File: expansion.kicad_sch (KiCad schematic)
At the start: 8 parts, among them J5 MEZZANINE, J7 PMOD_A, J8 PMOD_B

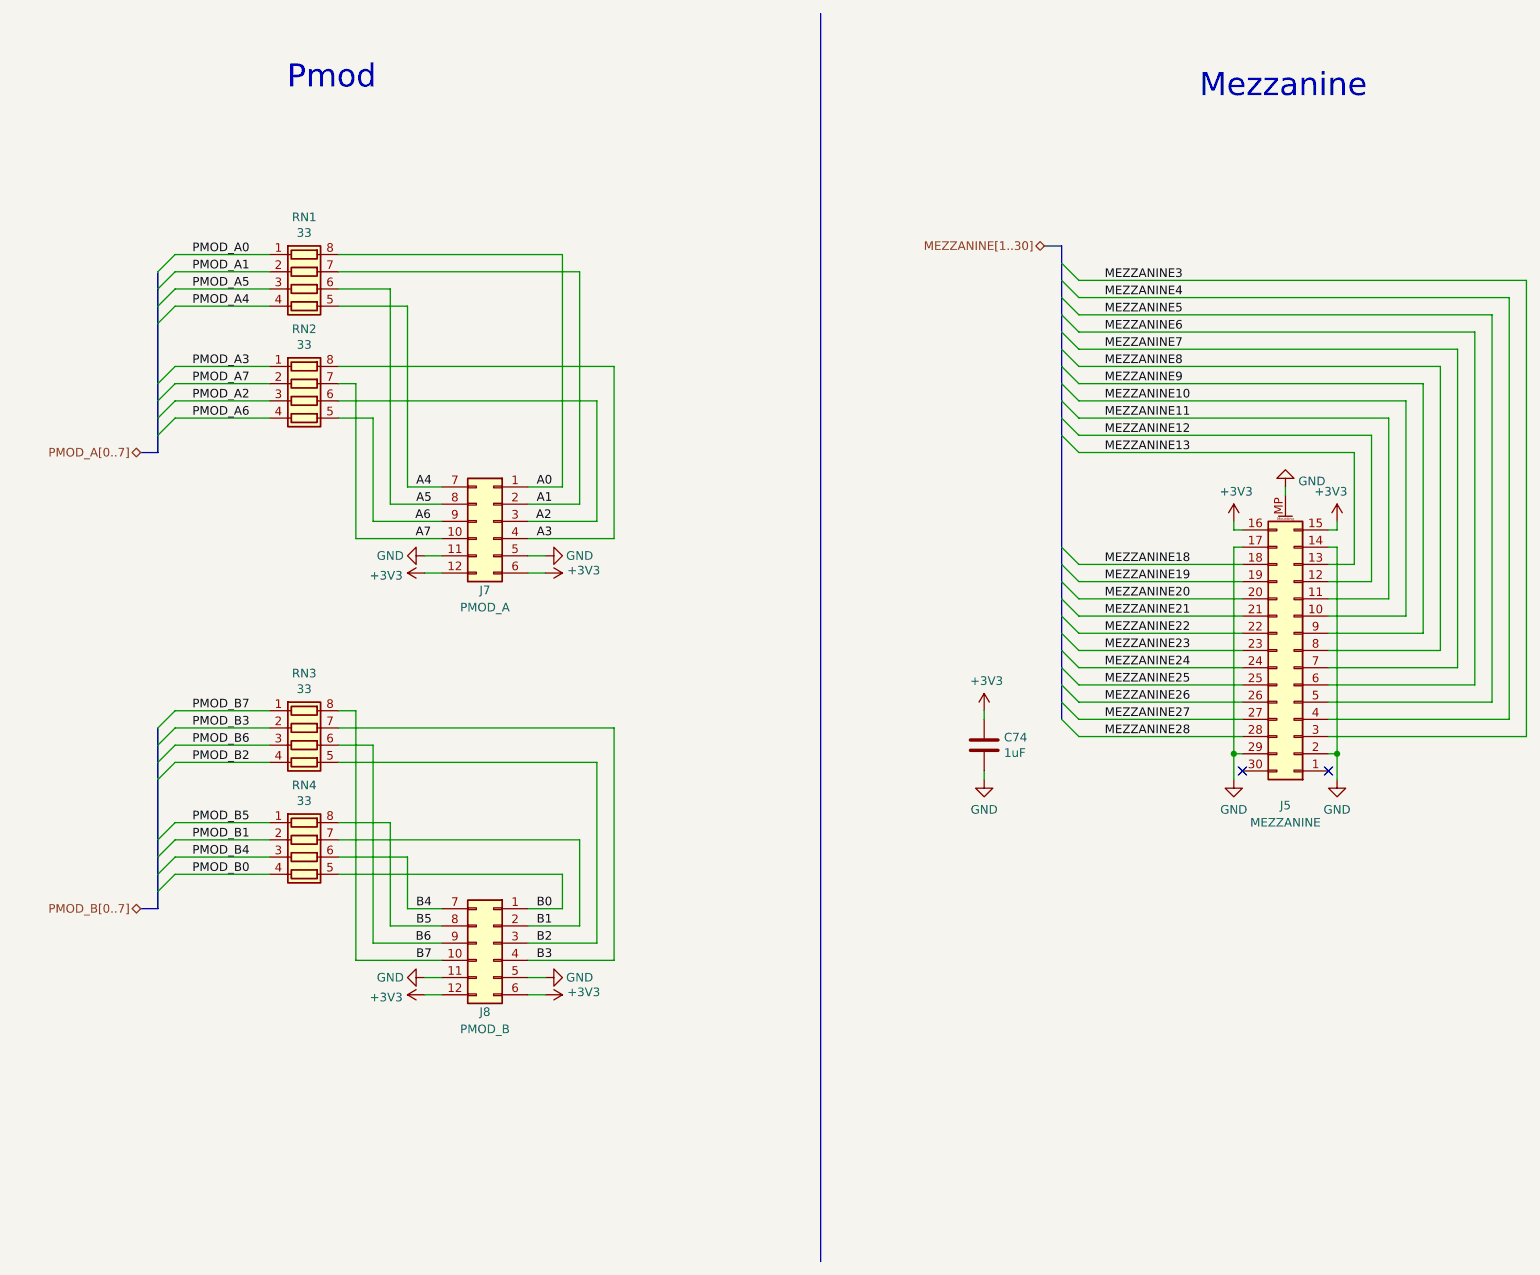
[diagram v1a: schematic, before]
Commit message: Clean up schematic
- Renumber Pmod signal names to match silkscreen labels
- Clean up FPGA symbol
- Clean up PHY symbol
- Add title block to newer sheets
- Fix horizontal line in LED sheet
- Improve various label positions
- Update data sheet fields
- Renumber pages
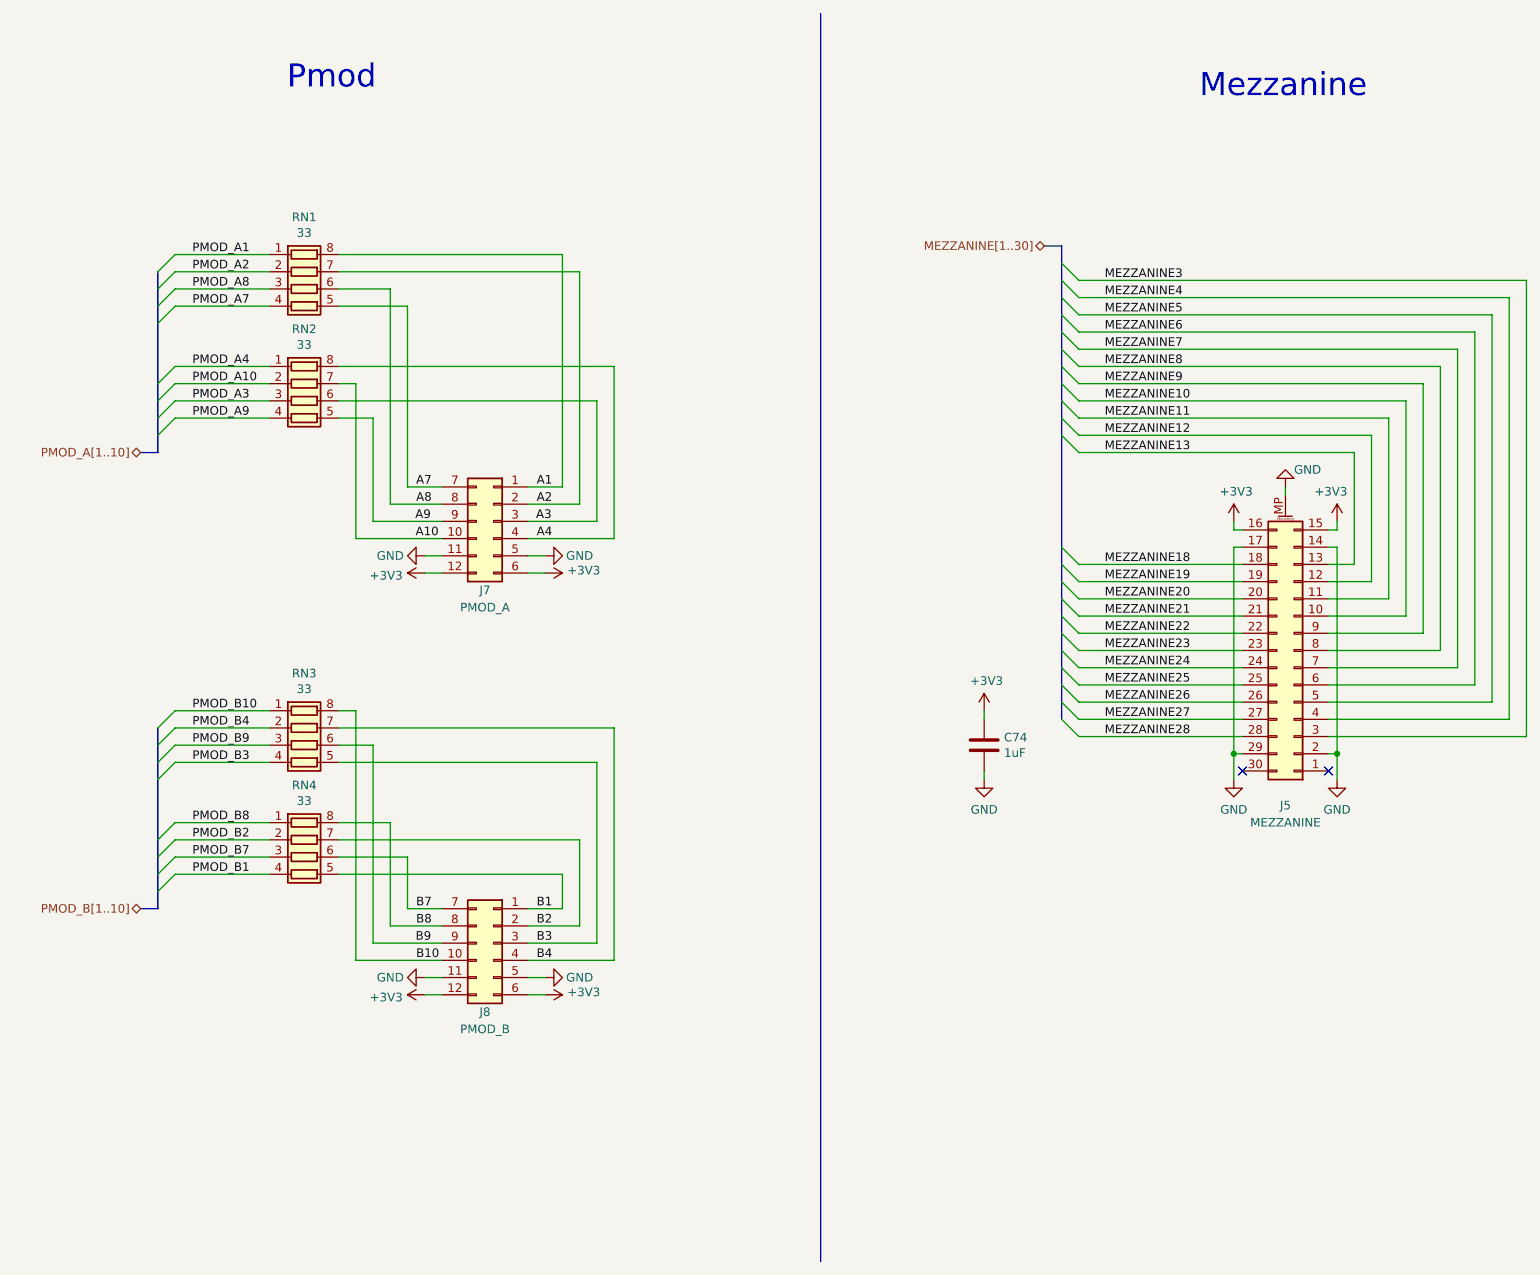
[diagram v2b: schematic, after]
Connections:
- net A0 is gone; now on net A1: J7.1 (Pin_1), RN1.8 (R1.2)
- net B0 is gone; now on net B1: J8.1 (Pin_1), RN4.5 (R4.2)
- net PMOD_A0 is gone; now on net PMOD_A1: RN1.1 (R1.1)
- net PMOD_B0 is gone; now on net PMOD_B1: RN4.4 (R4.1)
- net A1: no longer J7.2 (Pin_2), RN1.7 (R2.2)
- net A2: now also J7.2 (Pin_2), RN1.7 (R2.2); no longer J7.3 (Pin_3), RN2.6 (R3.2)
- net A3: now also J7.3 (Pin_3), RN2.6 (R3.2); no longer J7.4 (Pin_4), RN2.8 (R1.2)
- net A4: now also J7.4 (Pin_4), RN2.8 (R1.2); no longer J7.7 (Pin_7), RN1.5 (R4.2)
- net A7: now also J7.7 (Pin_7), RN1.5 (R4.2); no longer J7.10 (Pin_10), RN2.7 (R2.2)
- net B1: no longer J8.2 (Pin_2), RN4.7 (R2.2)
- net B2: now also J8.2 (Pin_2), RN4.7 (R2.2); no longer J8.3 (Pin_3), RN3.5 (R4.2)
- net B3: now also J8.3 (Pin_3), RN3.5 (R4.2); no longer J8.4 (Pin_4), RN3.7 (R2.2)
- net B4: now also J8.4 (Pin_4), RN3.7 (R2.2); no longer J8.7 (Pin_7), RN4.6 (R3.2)
- net B7: now also J8.7 (Pin_7), RN4.6 (R3.2); no longer J8.10 (Pin_10), RN3.8 (R1.2)
- net PMOD_A1: no longer RN1.2 (R2.1)
- net PMOD_A2: now also RN1.2 (R2.1); no longer RN2.3 (R3.1)
- net PMOD_A3: now also RN2.3 (R3.1); no longer RN2.1 (R1.1)
- net PMOD_A4: now also RN2.1 (R1.1); no longer RN1.4 (R4.1)
- net PMOD_A7: now also RN1.4 (R4.1); no longer RN2.2 (R2.1)
- net PMOD_B1: no longer RN4.2 (R2.1)
- net PMOD_B2: now also RN4.2 (R2.1); no longer RN3.4 (R4.1)
- net PMOD_B3: now also RN3.4 (R4.1); no longer RN3.2 (R2.1)
- net PMOD_B4: now also RN3.2 (R2.1); no longer RN4.3 (R3.1)
- net PMOD_B7: now also RN4.3 (R3.1); no longer RN3.1 (R1.1)
- net A5 renamed A8
- net A6 renamed A9
- net B5 renamed B8
- net B6 renamed B9
- net PMOD_A5 renamed PMOD_A8
- net PMOD_A6 renamed PMOD_A9
- net PMOD_B5 renamed PMOD_B8
- net PMOD_B6 renamed PMOD_B9
- new net A10: J7.10 (Pin_10), RN2.7 (R2.2)
- new net B10: J8.10 (Pin_10), RN3.8 (R1.2)
- new net PMOD_A10: RN2.2 (R2.1)
- new net PMOD_B10: RN3.1 (R1.1)
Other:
- company: (none) -> Copyright 2019-2023 Great Scott Gadgets
- title: (none) -> Cynthion
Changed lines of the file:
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@@
 (kicad_sch (version 20230121) (generator eeschema)
   (paper "A4")
+  (title_block
+    (title "Cynthion")
+    (date "${DATE}")
+    (rev "${VERSION}")
+    (company "Copyright 2019-2023 Great Scott Gadgets")
+    (comment 1 "Licensed under the CERN-OHL-P v2")
+  )
   (junction (at 228.6 121.92) (diameter 0) (color 0 0 0 0)
   )
@@
     (effects (font (size 1.27 1.27)) (justify left bottom))
   )
-  (label "B6" (at 92.6319 149.86 0) (fields_autoplaced)
+  (label "B9" (at 92.6319 149.86 0) (fields_autoplaced)
     (effects (font (size 1.27 1.27)) (justify left bottom))
   )
@@
     (effects (font (size 1.27 1.27)) (justify left bottom))
   )
-  (label "PMOD_A4" (at 59.69 55.88 0) (fields_autoplaced)
-    (effects (font (size 1.27 1.27)) (justify left bottom))
-  )
-  (label "PMOD_B3" (at 59.69 118.11 0) (fields_autoplaced)
-    (effects (font (size 1.27 1.27)) (justify left bottom))
-  )
-  (label "PMOD_B5" (at 59.69 132.08 0) (fields_autoplaced)
-    (effects (font (size 1.27 1.27)) (justify left bottom))
-  )
-  (label "A0" (at 110.49 82.55 0) (fields_autoplaced)
-    (effects (font (size 1.27 1.27)) (justify left bottom))
-  )
-  (label "A1" (at 110.49 85.09 0) (fields_autoplaced)
-    (effects (font (size 1.27 1.27)) (justify left bottom))
-  )
-  (label "PMOD_A2" (at 59.69 69.85 0) (fields_autoplaced)
+  (label "PMOD_A7" (at 59.69 55.88 0) (fields_autoplaced)
+    (effects (font (size 1.27 1.27)) (justify left bottom))
+  )
+  (label "PMOD_B4" (at 59.69 118.11 0) (fields_autoplaced)
+    (effects (font (size 1.27 1.27)) (justify left bottom))
+  )
+  (label "PMOD_B8" (at 59.69 132.08 0) (fields_autoplaced)
+    (effects (font (size 1.27 1.27)) (justify left bottom))
+  )
+  (label "A1" (at 110.49 82.55 0) (fields_autoplaced)
+    (effects (font (size 1.27 1.27)) (justify left bottom))
+  )
+  (label "A2" (at 110.49 85.09 0) (fields_autoplaced)
+    (effects (font (size 1.27 1.27)) (justify left bottom))
+  )
+  (label "PMOD_A3" (at 59.69 69.85 0) (fields_autoplaced)
     (effects (font (size 1.27 1.27)) (justify left bottom))
   )
@@
     (effects (font (size 1.27 1.27)) (justify left bottom))
   )
-  (label "PMOD_B0" (at 59.69 139.7 0) (fields_autoplaced)
-    (effects (font (size 1.27 1.27)) (justify left bottom))
-  )
-  (label "A5" (at 92.71 85.09 0) (fields_autoplaced)
-    (effects (font (size 1.27 1.27)) (justify left bottom))
-  )
-  (label "PMOD_A0" (at 59.69 48.26 0) (fields_autoplaced)
+  (label "PMOD_B1" (at 59.69 139.7 0) (fields_autoplaced)
+    (effects (font (size 1.27 1.27)) (justify left bottom))
+  )
+  (label "A8" (at 92.71 85.09 0) (fields_autoplaced)
+    (effects (font (size 1.27 1.27)) (justify left bottom))
+  )
+  (label "PMOD_A1" (at 59.69 48.26 0) (fields_autoplaced)
     (effects (font (size 1.27 1.27)) (justify left bottom))
   )
@@
     (effects (font (size 1.27 1.27)) (justify left bottom))
   )
-  (label "PMOD_B6" (at 59.69 120.65 0) (fields_autoplaced)
-    (effects (font (size 1.27 1.27)) (justify left bottom))
-  )
-  (label "PMOD_B1" (at 59.69 134.62 0) (fields_autoplaced)
+  (label "PMOD_B9" (at 59.69 120.65 0) (fields_autoplaced)
+    (effects (font (size 1.27 1.27)) (justify left bottom))
+  )
+  (label "PMOD_B2" (at 59.69 134.62 0) (fields_autoplaced)
     (effects (font (size 1.27 1.27)) (justify left bottom))
   )
@@
     (effects (font (size 1.27 1.27)) (justify left bottom))
   )
-  (label "PMOD_B4" (at 59.69 137.16 0) (fields_autoplaced)
-    (effects (font (size 1.27 1.27)) (justify left bottom))
-  )
-  (label "B5" (at 92.71 147.32 0) (fields_autoplaced)
-    (effects (font (size 1.27 1.27)) (justify left bottom))
-  )
-  (label "PMOD_B7" (at 59.69 115.57 0) (fields_autoplaced)
-    (effects (font (size 1.27 1.27)) (justify left bottom))
-  )
-  (label "B4" (at 92.71 144.78 0) (fields_autoplaced)
-    (effects (font (size 1.27 1.27)) (justify left bottom))
-  )
-  (label "B3" (at 110.49 152.4 0) (fields_autoplaced)
-    (effects (font (size 1.27 1.27)) (justify left bottom))
-  )
-  (label "PMOD_A1" (at 59.69 50.8 0) (fields_autoplaced)
+  (label "PMOD_B7" (at 59.69 137.16 0) (fields_autoplaced)
+    (effects (font (size 1.27 1.27)) (justify left bottom))
+  )
+  (label "B8" (at 92.71 147.32 0) (fields_autoplaced)
+    (effects (font (size 1.27 1.27)) (justify left bottom))
+  )
+  (label "PMOD_B10" (at 59.69 115.57 0) (fields_autoplaced)
+    (effects (font (size 1.27 1.27)) (justify left bottom))
+  )
+  (label "B7" (at 92.71 144.78 0) (fields_autoplaced)
+    (effects (font (size 1.27 1.27)) (justify left bottom))
+  )
+  (label "B4" (at 110.49 152.4 0) (fields_autoplaced)
+    (effects (font (size 1.27 1.27)) (justify left bottom))
+  )
+  (label "PMOD_A2" (at 59.69 50.8 0) (fields_autoplaced)
     (effects (font (size 1.27 1.27)) (justify left bottom))
   )
@@
     (effects (font (size 1.27 1.27)) (justify left bottom))
   )
-  (label "A6" (at 92.5802 87.63 0) (fields_autoplaced)
-    (effects (font (size 1.27 1.27)) (justify left bottom))
-  )
-  (label "PMOD_B2" (at 59.69 123.19 0) (fields_autoplaced)
-    (effects (font (size 1.27 1.27)) (justify left bottom))
-  )
-  (label "PMOD_A6" (at 59.69 72.39 0) (fields_autoplaced)
+  (label "A9" (at 92.5802 87.63 0) (fields_autoplaced)
+    (effects (font (size 1.27 1.27)) (justify left bottom))
+  )
+  (label "PMOD_B3" (at 59.69 123.19 0) (fields_autoplaced)
+    (effects (font (size 1.27 1.27)) (justify left bottom))
+  )
+  (label "PMOD_A9" (at 59.69 72.39 0) (fields_autoplaced)
     (effects (font (size 1.27 1.27)) (justify left bottom))
   )
@@
     (effects (font (size 1.27 1.27)) (justify left bottom))
   )
-  (label "PMOD_A5" (at 59.69 53.34 0) (fields_autoplaced)
-    (effects (font (size 1.27 1.27)) (justify left bottom))
-  )
-  (label "B7" (at 92.71 152.4 0) (fields_autoplaced)
-    (effects (font (size 1.27 1.27)) (justify left bottom))
-  )
-  (label "B0" (at 110.49 144.78 0) (fields_autoplaced)
+  (label "PMOD_A8" (at 59.69 53.34 0) (fields_autoplaced)
+    (effects (font (size 1.27 1.27)) (justify left bottom))
+  )
+  (label "B10" (at 92.71 152.4 0) (fields_autoplaced)
+    (effects (font (size 1.27 1.27)) (justify left bottom))
+  )
+  (label "B1" (at 110.49 144.78 0) (fields_autoplaced)
     (effects (font (size 1.27 1.27)) (justify left bottom))
   )
@@
     (effects (font (size 1.27 1.27)) (justify left bottom))
   )
-  (label "A7" (at 92.6242 90.17 0) (fields_autoplaced)
+  (label "A10" (at 92.6242 90.17 0) (fields_autoplaced)
     (effects (font (size 1.27 1.27)) (justify left bottom))
   )
@@
     (effects (font (size 1.27 1.27)) (justify left bottom))
   )
-  (label "A4" (at 92.71 82.55 0) (fields_autoplaced)
-    (effects (font (size 1.27 1.27)) (justify left bottom))
-  )
-  (label "B2" (at 110.49 149.86 0) (fields_autoplaced)
-    (effects (font (size 1.27 1.27)) (justify left bottom))
-  )
-  (label "A2" (at 110.3963 87.63 0) (fields_autoplaced)
+  (label "A7" (at 92.71 82.55 0) (fields_autoplaced)
+    (effects (font (size 1.27 1.27)) (justify left bottom))
+  )
+  (label "B3" (at 110.49 149.86 0) (fields_autoplaced)
+    (effects (font (size 1.27 1.27)) (justify left bottom))
+  )
+  (label "A3" (at 110.3963 87.63 0) (fields_autoplaced)
     (effects (font (size 1.27 1.27)) (justify left bottom))
   )
@@
     (effects (font (size 1.27 1.27)) (justify left bottom))
   )
-  (label "B1" (at 110.49 147.32 0) (fields_autoplaced)
-    (effects (font (size 1.27 1.27)) (justify left bottom))
-  )
-  (label "PMOD_A3" (at 59.69 64.77 0) (fields_autoplaced)
+  (label "B2" (at 110.49 147.32 0) (fields_autoplaced)
+    (effects (font (size 1.27 1.27)) (justify left bottom))
+  )
+  (label "PMOD_A4" (at 59.69 64.77 0) (fields_autoplaced)
     (effects (font (size 1.27 1.27)) (justify left bottom))
   )
@@
     (effects (font (size 1.27 1.27)) (justify left bottom))
   )
-  (label "PMOD_A7" (at 59.69 67.31 0) (fields_autoplaced)
-    (effects (font (size 1.27 1.27)) (justify left bottom))
-  )
-  (label "A3" (at 110.49 90.17 0) (fields_autoplaced)
+  (label "PMOD_A10" (at 59.69 67.31 0) (fields_autoplaced)
+    (effects (font (size 1.27 1.27)) (justify left bottom))
+  )
+  (label "A4" (at 110.49 90.17 0) (fields_autoplaced)
     (effects (font (size 1.27 1.27)) (justify left bottom))
   )
@@
     (effects (font (size 1.27 1.27)) (justify left bottom))
   )
-  (hierarchical_label "PMOD_B[0..7]" (shape bidirectional) (at 52.07 144.78 180) (fields_autoplaced)
+  (hierarchical_label "PMOD_B[1..10]" (shape bidirectional) (at 52.07 144.78 180) (fields_autoplaced)
     (effects (font (size 1.27 1.27)) (justify right))
   )
-  (hierarchical_label "PMOD_A[0..7]" (shape bidirectional) (at 52.07 77.47 180) (fields_autoplaced)
+  (hierarchical_label "PMOD_A[1..10]" (shape bidirectional) (at 52.07 77.47 180) (fields_autoplaced)
     (effects (font (size 1.27 1.27)) (justify right))
   )
@@
       (effects (font (size 1.27 1.27)) hide)
     )
-    (property "Datasheet" "~" (at 222.25 106.68 0)
+    (property "Datasheet" "https://cdn.amphenol-cs.com/media/wysiwyg/files/drawing/10132798.pdf" (at 222.25 106.68 0)
       (effects (font (size 1.27 1.27)) hide)
     )
@@
   )
   (symbol (lib_id "power:GND") (at 220.98 82.55 180) (unit 1)
-    (in_bom yes) (on_board yes) (dnp no) (fields_autoplaced)
+    (in_bom yes) (on_board yes) (dnp no)
     (property "Reference" "#PWR074" (at 220.98 76.2 0)
       (effects (font (size 1.27 1.27)) hide)
     )
-    (property "Value" "GND" (at 222.885 81.7138 0)
+    (property "Value" "GND" (at 222.25 80.01 0)
       (effects (font (size 1.27 1.27)) (justify right))
     )

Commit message: Update copyright notices
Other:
- company: Copyright 2019-2023 Great Scott Gadgets -> ${COPYRIGHT}
- title: Cynthion -> ${TITLE}
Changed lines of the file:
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@@
   (paper "A4")
   (title_block
-    (title "Cynthion")
+    (title "${TITLE}")
     (date "${DATE}")
     (rev "${VERSION}")
-    (company "Copyright 2019-2023 Great Scott Gadgets")
-    (comment 1 "Licensed under the CERN-OHL-P v2")
+    (company "${COPYRIGHT}")
+    (comment 1 "${LICENSE}")
   )
   (junction (at 228.6 121.92) (diameter 0) (color 0 0 0 0)
